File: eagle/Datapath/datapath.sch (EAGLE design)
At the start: 0 parts

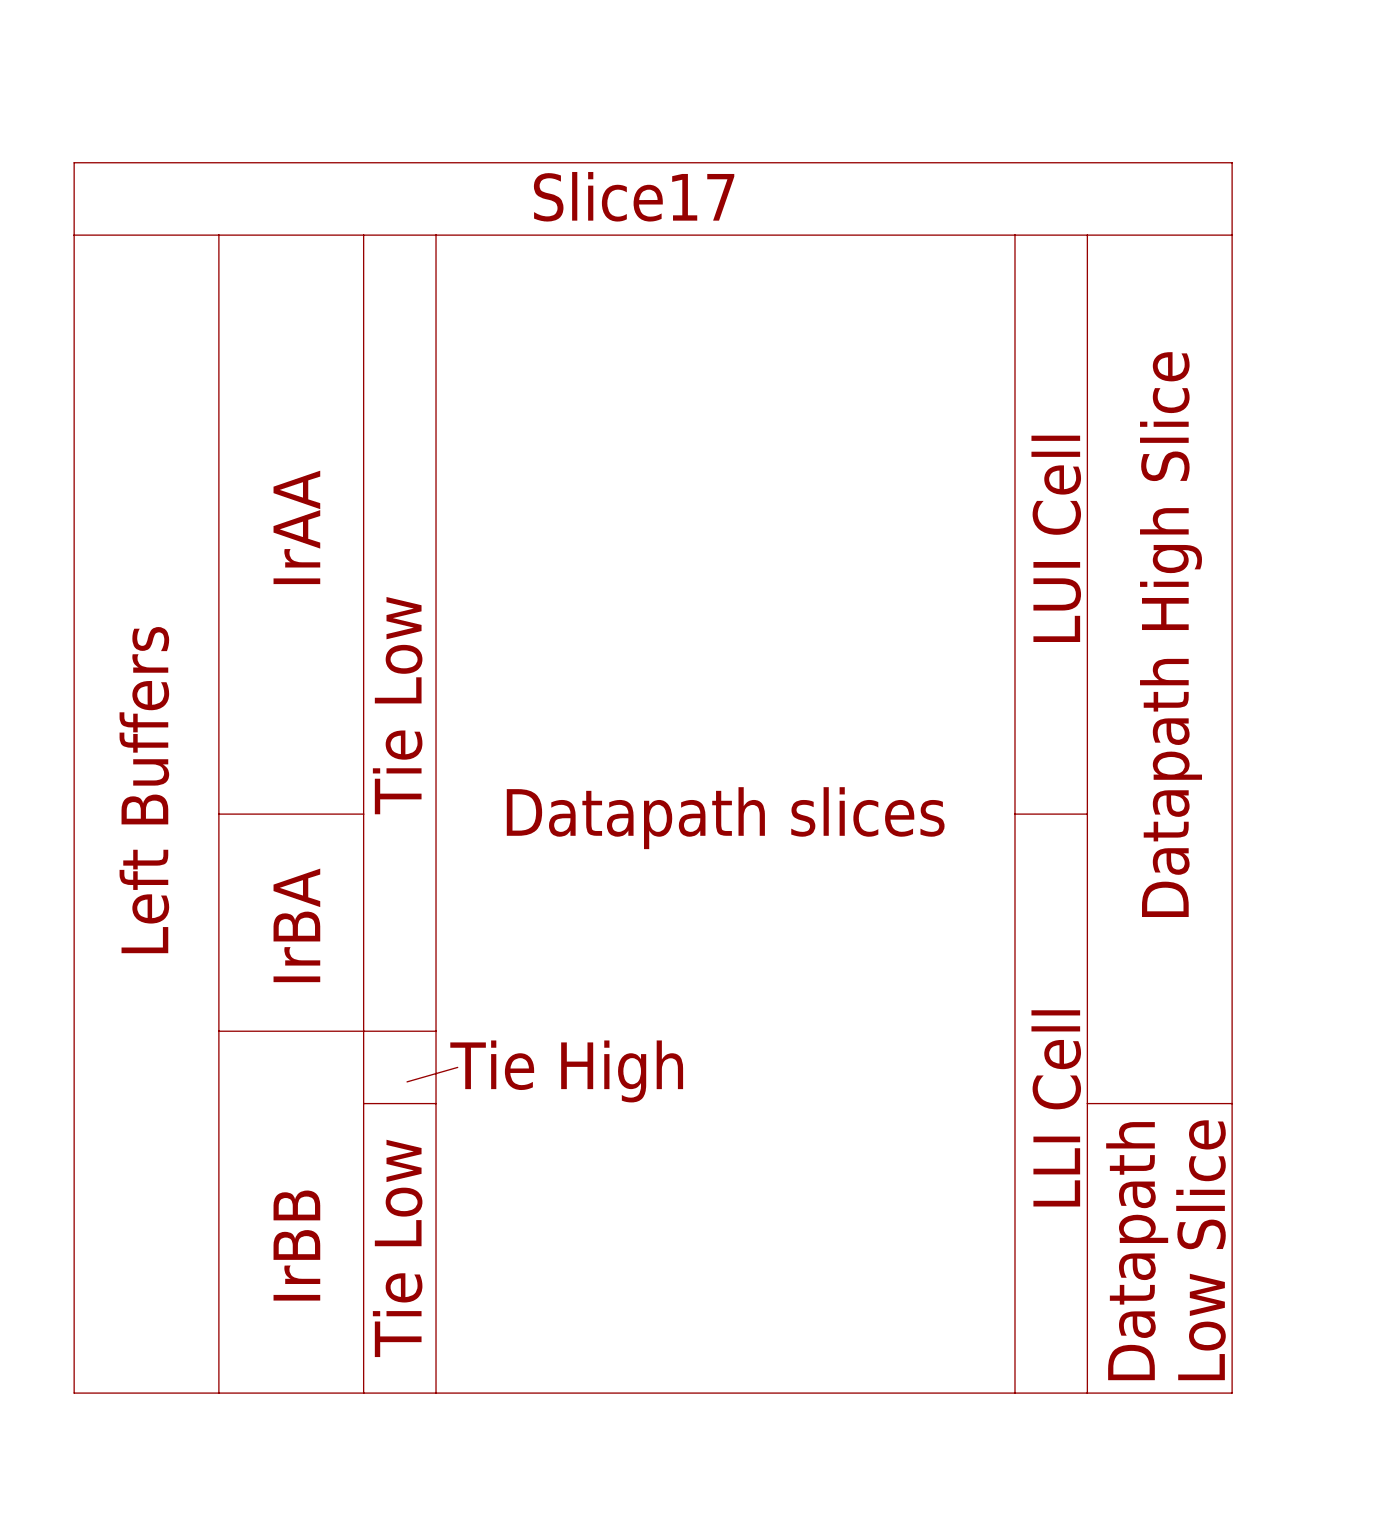
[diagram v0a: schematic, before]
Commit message: Done a little more on the datapath and draft of the CPU design.
Can't think of much more to put in the CPU design. #96
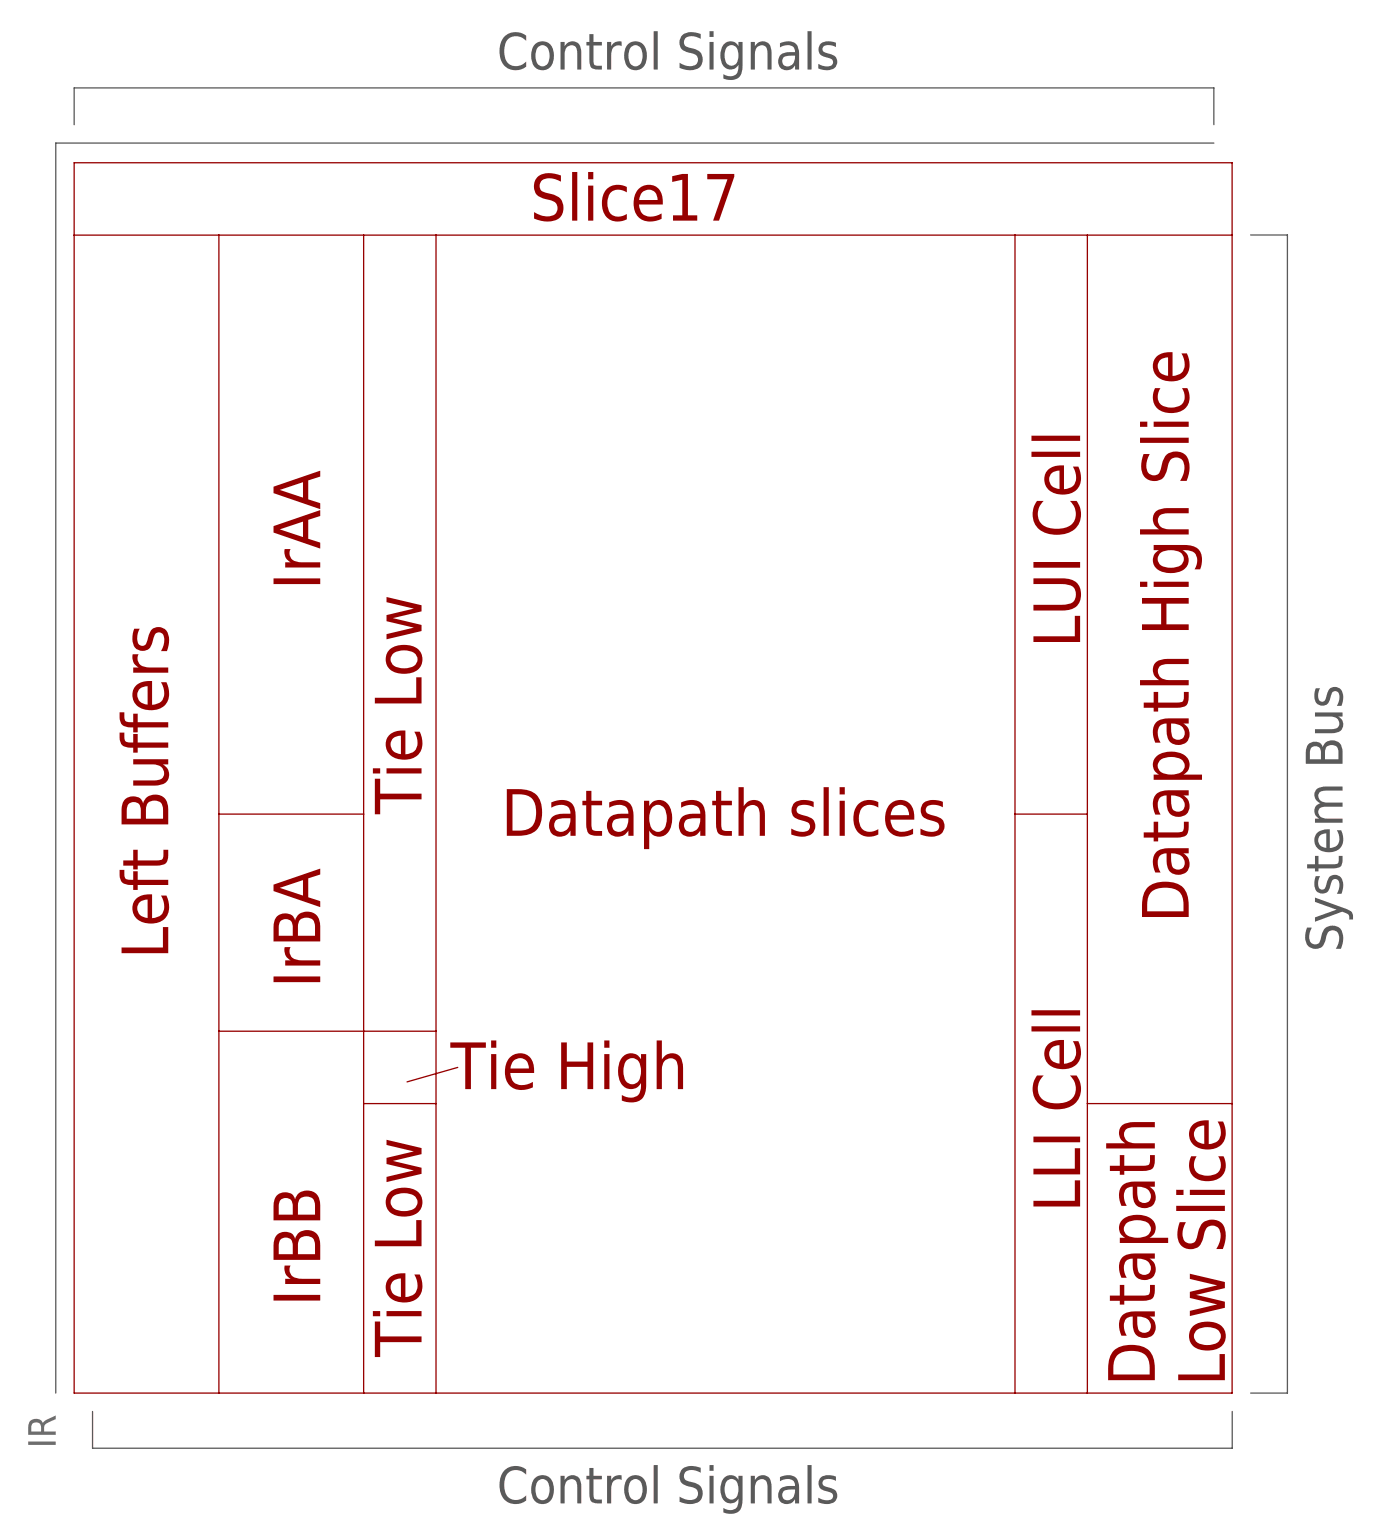
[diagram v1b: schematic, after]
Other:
- note added: "Control Signals"
- note added: "System Bus"
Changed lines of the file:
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@@
 <?xml version="1.0" encoding="utf-8"?>
 <!DOCTYPE eagle SYSTEM "eagle.dtd">
-<eagle version="6.5.0">
+<eagle version="6.3">
 <drawing>
 <settings>
@@
 <setting verticaltext="up"/>
 </settings>
-<grid distance="1" unitdist="mm" unit="mm" style="lines" multiple="1" display="yes" altdistance="1" altunitdist="mm" altunit="mm"/>
+<grid distance="0.1" unitdist="inch" unit="inch" style="lines" multiple="1" display="no" altdistance="0.01" altunitdist="inch" altunit="inch"/>
 <layers>
 <layer number="91" name="Nets" color="2" fill="1" visible="yes" active="yes"/>
@@
 <wire x1="53" y1="45" x2="46" y2="43" width="0.1524" layer="94"/>
 <text x="63" y="162" size="6.4516" layer="94">Slice17</text>
+<wire x1="162.56" y1="160.02" x2="167.64" y2="160.02" width="0.1524" layer="97"/>
+<wire x1="167.64" y1="160.02" x2="167.64" y2="0" width="0.1524" layer="97"/>
+<wire x1="167.64" y1="0" x2="162.56" y2="0" width="0.1524" layer="97"/>
+<text x="175.26" y="60.96" size="5.08" layer="97" rot="R90">System Bus</text>
+<text x="58.42" y="-15.24" size="5.08" layer="97">Control Signals</text>
+<text x="58.42" y="182.88" size="5.08" layer="97">Control Signals</text>
+<wire x1="0" y1="175.26" x2="0" y2="180.34" width="0.1524" layer="97"/>
+<wire x1="0" y1="180.34" x2="157.48" y2="180.34" width="0.1524" layer="97"/>
+<wire x1="157.48" y1="180.34" x2="157.48" y2="175.26" width="0.1524" layer="97"/>
+<wire x1="2.54" y1="-2.54" x2="2.54" y2="-7.62" width="0.1524" layer="97"/>
+<wire x1="2.54" y1="-7.62" x2="160.02" y2="-7.62" width="0.1524" layer="97"/>
+<wire x1="160.02" y1="-7.62" x2="160.02" y2="-2.54" width="0.1524" layer="97"/>
 </plain>
 <instances>
 </instances>
 <busses>
+<bus name="IR">
+<segment>
+<wire x1="-2.54" y1="0" x2="-2.54" y2="172.72" width="0.762" layer="92"/>
+<wire x1="-2.54" y1="172.72" x2="157.48" y2="172.72" width="0.762" layer="92"/>
+<label x="-2.54" y="-7.62" size="3.81" layer="95" rot="R90"/>
+</segment>
+</bus>
 </busses>
 <nets>
